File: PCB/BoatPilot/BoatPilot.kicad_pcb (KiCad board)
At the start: 2 copper layers, 40 x 40 mm, 83 parts, among them J101 battery, J102 switch, J103 SWD, J104 wind, J105 RC, J106 GPS, J108 failsafe, J109 SERVO1, J110 SERVO2, J111 SERVO3, J201 GPIO, J202 USB-Audio-IR, J203 Audio-UART, P101 ICT-Point, P102 ICT-Point, P103 ICT-Point, P104 ICT-Point, P105 ICT-Point, P113 ICT-Point, P119 ICT-Point, P129 ICT-Point, P130 ICT-Point, P132 ICT-Point, P133 ICT-Point, P134 ICT-Point, P135 ICT-Point, Q101 TSM3457, U101 GY-91, U102 74LVC1G97, U103 LM1117-3.3, U104 TPS565208, U105 24LC512, U106 74LVC1G97, U108 74LVC1G97, U109 STM32F103C8Tx, Y101 8MHz

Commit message: Finish documentation
Documentation layer finished
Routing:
- net GND: vias 79 -> 75

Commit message: Move Servo outputs
Move servo outputs so that only a single Timer (TIM2) is needed to
gerenarte the PWM with the Capture Compare units.
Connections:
- J201 pad 10: (no net) -> /FriednlyARM NanoPi Air/RX1
- J201 pad 13: (no net) -> /FriednlyARM NanoPi Air/RTS2_PA2
- J201 pad 15: (no net) -> /FriednlyARM NanoPi Air/CTS2_PA3
- J201 pad 16: (no net) -> /FriednlyARM NanoPi Air/RTS1
- J201 pad 18: (no net) -> /FriednlyARM NanoPi Air/CTS1
- J201 pad 7: (no net) -> /FriednlyARM NanoPi Air/PG11
- J201 pad 8: (no net) -> /FriednlyARM NanoPi Air/TX1
- J202 pad 10: (no net) -> /FriednlyARM NanoPi Air/I2S_DOUT
- J202 pad 11: (no net) -> /FriednlyARM NanoPi Air/I2S_DIN
- J202 pad 2: (no net) -> /FriednlyARM NanoPi Air/D1P
- J202 pad 3: (no net) -> /FriednlyARM NanoPi Air/D1N
- J202 pad 6: (no net) -> /FriednlyARM NanoPi Air/PL11_IR
- J202 pad 7: (no net) -> /FriednlyARM NanoPi Air/PA17_SPDIF
- J202 pad 8: (no net) -> /FriednlyARM NanoPi Air/I2S_LRCK
- J202 pad 9: (no net) -> /FriednlyARM NanoPi Air/I2S_BCK
- J203 pad 3: (no net) -> /FriednlyARM NanoPi Air/TX0
- J203 pad 4: (no net) -> /FriednlyARM NanoPi Air/RX0
- J203 pad 5: (no net) -> /FriednlyARM NanoPi Air/LL
- J203 pad 6: (no net) -> /FriednlyARM NanoPi Air/LR
- J203 pad 7: (no net) -> /FriednlyARM NanoPi Air/MN
- J203 pad 8: (no net) -> /FriednlyARM NanoPi Air/MP
- U101 pad 1: (no net) -> Net-(U101-Pad1)
- U109 pad 11: (no net) -> Net-(U109-Pad11)
- U109 pad 18: (no net) -> Net-(U109-Pad18)
- U109 pad 19: (no net) -> Net-(U109-Pad19)
- U109 pad 2: (no net) -> Net-(U109-Pad2)
- U109 pad 20: (no net) -> Net-(U109-Pad20)
- U109 pad 21: (no net) -> Net-(U109-Pad21)
- U109 pad 22: (no net) -> Net-(U109-Pad22)
- U109 pad 25: (no net) -> Net-(U109-Pad25)
- U109 pad 3: (no net) -> Net-(U109-Pad3)
- U109 pad 38: (no net) -> Net-(U109-Pad38)
- U109 pad 4: (no net) -> Net-(U109-Pad4)
- U109 pad 46: (no net) -> Net-(U109-Pad46)
- Y101 pad 2: (no net) -> Net-(Y101-Pad2)
- Y101 pad 4: (no net) -> Net-(Y101-Pad4)
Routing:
- net GND: track 70.7 -> 72.0 mm

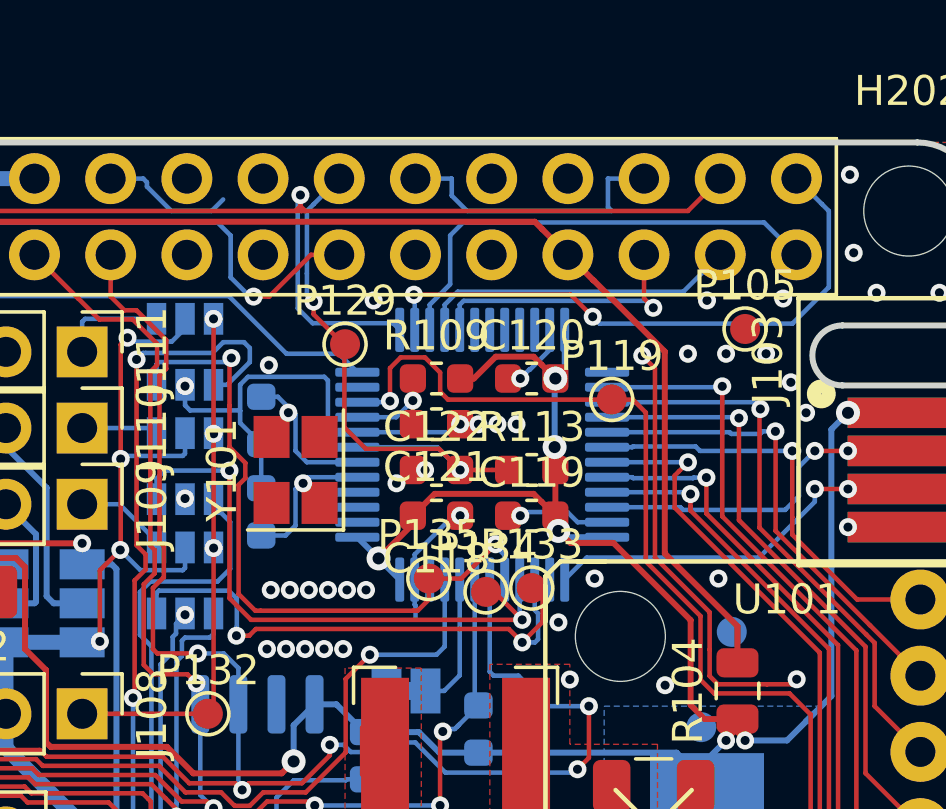
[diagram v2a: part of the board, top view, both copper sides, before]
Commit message: Route new servo connections
Reroute parts of the PCB to fit the new servo connections
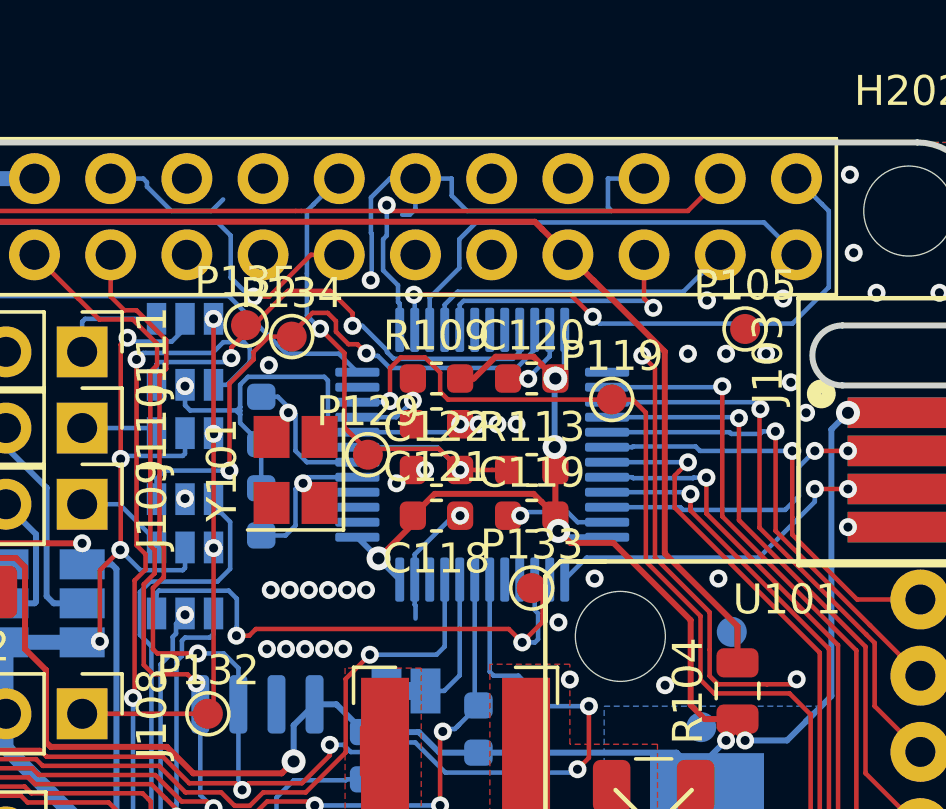
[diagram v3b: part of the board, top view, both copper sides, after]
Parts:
- moved P134 10.7 mm to (141.1, 85.5)
- moved P135 10.4 mm to (139.6, 85.1)
- moved P129 3.76 mm to (143.7, 89.4)
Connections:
- J201 pad 10: /FriednlyARM NanoPi Air/RX1 -> (no net)
- J201 pad 13: /FriednlyARM NanoPi Air/RTS2_PA2 -> (no net)
- J201 pad 15: /FriednlyARM NanoPi Air/CTS2_PA3 -> (no net)
- J201 pad 16: /FriednlyARM NanoPi Air/RTS1 -> (no net)
- J201 pad 18: /FriednlyARM NanoPi Air/CTS1 -> (no net)
- J201 pad 7: /FriednlyARM NanoPi Air/PG11 -> (no net)
- J201 pad 8: /FriednlyARM NanoPi Air/TX1 -> (no net)
- J202 pad 10: /FriednlyARM NanoPi Air/I2S_DOUT -> (no net)
- J202 pad 11: /FriednlyARM NanoPi Air/I2S_DIN -> (no net)
- J202 pad 2: /FriednlyARM NanoPi Air/D1P -> (no net)
- J202 pad 3: /FriednlyARM NanoPi Air/D1N -> (no net)
- J202 pad 6: /FriednlyARM NanoPi Air/PL11_IR -> (no net)
- J202 pad 7: /FriednlyARM NanoPi Air/PA17_SPDIF -> (no net)
- J202 pad 8: /FriednlyARM NanoPi Air/I2S_LRCK -> (no net)
- J202 pad 9: /FriednlyARM NanoPi Air/I2S_BCK -> (no net)
- J203 pad 3: /FriednlyARM NanoPi Air/TX0 -> (no net)
- J203 pad 4: /FriednlyARM NanoPi Air/RX0 -> (no net)
- J203 pad 5: /FriednlyARM NanoPi Air/LL -> (no net)
- J203 pad 6: /FriednlyARM NanoPi Air/LR -> (no net)
- J203 pad 7: /FriednlyARM NanoPi Air/MN -> (no net)
- J203 pad 8: /FriednlyARM NanoPi Air/MP -> (no net)
- U101 pad 1: Net-(U101-Pad1) -> (no net)
- U109 pad 11: Net-(U109-Pad11) -> (no net)
- U109 pad 18: Net-(U109-Pad18) -> (no net)
- U109 pad 19: Net-(U109-Pad19) -> (no net)
- U109 pad 2: Net-(U109-Pad2) -> (no net)
- U109 pad 20: Net-(U109-Pad20) -> (no net)
- U109 pad 21: Net-(U109-Pad21) -> /SERVO3
- U109 pad 22: Net-(U109-Pad22) -> /SERVO1
- U109 pad 25: Net-(U109-Pad25) -> (no net)
- U109 pad 3: Net-(U109-Pad3) -> (no net)
- U109 pad 38: Net-(U109-Pad38) -> (no net)
- U109 pad 4: Net-(U109-Pad4) -> (no net)
- U109 pad 40: /SERVO1 -> (no net)
- U109 pad 41: /SERVO3 -> (no net)
- U109 pad 46: Net-(U109-Pad46) -> (no net)
- Y101 pad 2: Net-(Y101-Pad2) -> (no net)
- Y101 pad 4: Net-(Y101-Pad4) -> (no net)
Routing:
- net GND: track 72.0 -> 79.6 mm
- net /SERVO3: track 22.9 -> 16.5 mm
- net /UART2_RX: track 49.4 -> 45.5 mm
- net /SERVO1: track 20.5 -> 19.4 mm

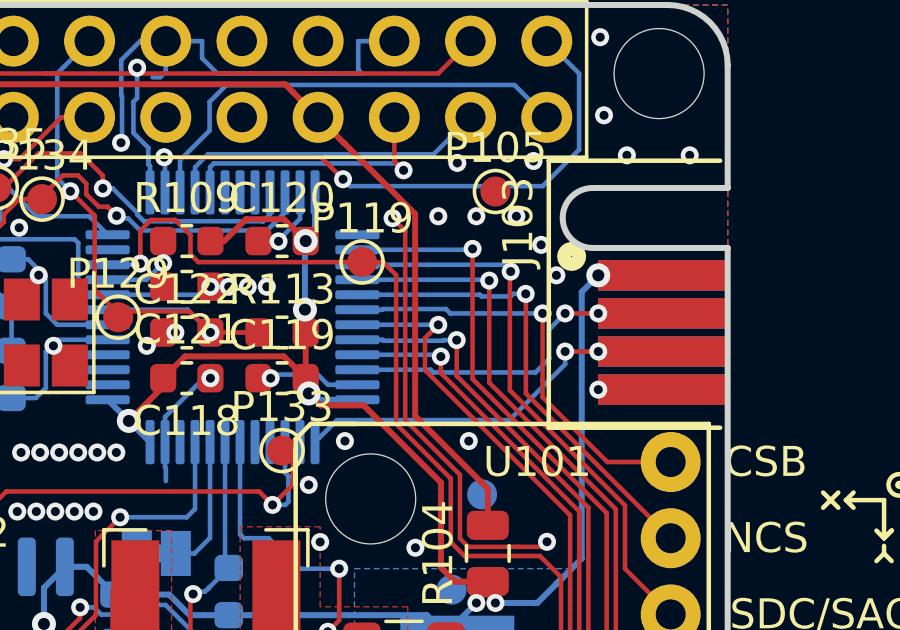
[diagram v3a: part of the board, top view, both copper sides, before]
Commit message: Swap UART1 RX and TX to enable half duplex mode
In half duplex mode, UART RX can be used as a GPIO pin. So the pinning
on the uC has to be swapped.
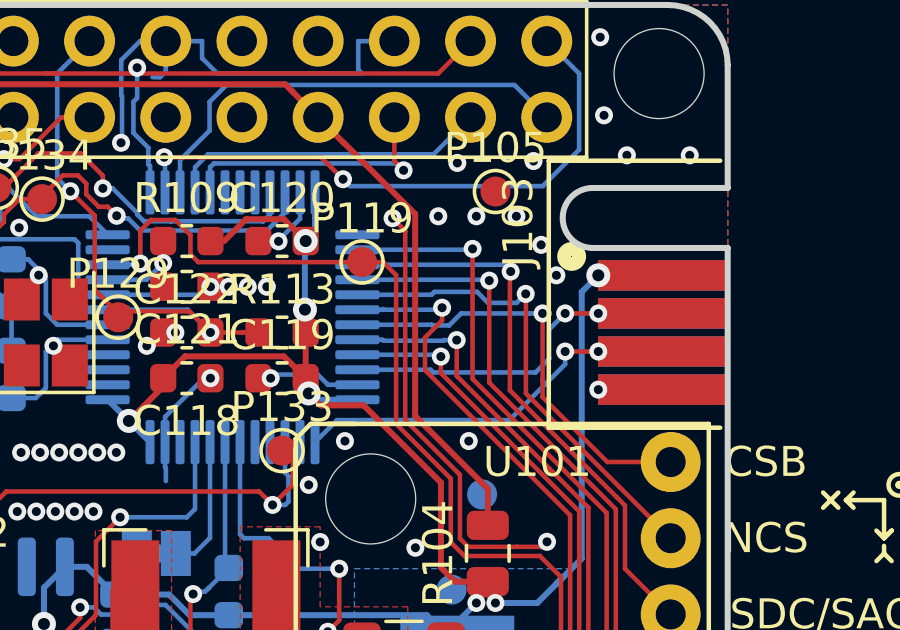
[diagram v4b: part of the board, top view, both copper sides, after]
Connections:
- J201 pad 10: (no net) -> /FriednlyARM NanoPi Air/RX1
- J201 pad 13: (no net) -> /FriednlyARM NanoPi Air/RTS2_PA2
- J201 pad 15: (no net) -> /FriednlyARM NanoPi Air/CTS2_PA3
- J201 pad 16: (no net) -> /FriednlyARM NanoPi Air/RTS1
- J201 pad 18: (no net) -> /FriednlyARM NanoPi Air/CTS1
- J201 pad 7: (no net) -> /FriednlyARM NanoPi Air/PG11
- J201 pad 8: (no net) -> /FriednlyARM NanoPi Air/TX1
- J202 pad 10: (no net) -> /FriednlyARM NanoPi Air/I2S_DOUT
- J202 pad 11: (no net) -> /FriednlyARM NanoPi Air/I2S_DIN
- J202 pad 2: (no net) -> /FriednlyARM NanoPi Air/D1P
- J202 pad 3: (no net) -> /FriednlyARM NanoPi Air/D1N
- J202 pad 6: (no net) -> /FriednlyARM NanoPi Air/PL11_IR
- J202 pad 7: (no net) -> /FriednlyARM NanoPi Air/PA17_SPDIF
- J202 pad 8: (no net) -> /FriednlyARM NanoPi Air/I2S_LRCK
- J202 pad 9: (no net) -> /FriednlyARM NanoPi Air/I2S_BCK
- J203 pad 3: (no net) -> /FriednlyARM NanoPi Air/TX0
- J203 pad 4: (no net) -> /FriednlyARM NanoPi Air/RX0
- J203 pad 5: (no net) -> /FriednlyARM NanoPi Air/LL
- J203 pad 6: (no net) -> /FriednlyARM NanoPi Air/LR
- J203 pad 7: (no net) -> /FriednlyARM NanoPi Air/MN
- J203 pad 8: (no net) -> /FriednlyARM NanoPi Air/MP
- U101 pad 1: (no net) -> Net-(U101-Pad1)
- U109 pad 11: (no net) -> Net-(U109-Pad11)
- U109 pad 18: (no net) -> Net-(U109-Pad18)
- U109 pad 19: (no net) -> Net-(U109-Pad19)
- U109 pad 2: (no net) -> Net-(U109-Pad2)
- U109 pad 20: (no net) -> Net-(U109-Pad20)
- U109 pad 25: (no net) -> Net-(U109-Pad25)
- U109 pad 3: (no net) -> Net-(U109-Pad3)
- U109 pad 30: /~CS_MPU9250 -> /RC_IBUS
- U109 pad 31: /RC_IBUS -> /~CS_MPU9250
- U109 pad 38: (no net) -> Net-(U109-Pad38)
- U109 pad 4: (no net) -> Net-(U109-Pad4)
- U109 pad 40: (no net) -> Net-(U109-Pad40)
- U109 pad 41: (no net) -> Net-(U109-Pad41)
- U109 pad 46: (no net) -> Net-(U109-Pad46)
- Y101 pad 2: (no net) -> Net-(Y101-Pad2)
- Y101 pad 4: (no net) -> Net-(Y101-Pad4)
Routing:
- net /RC_IBUS: track 54.1 -> 54.9 mm

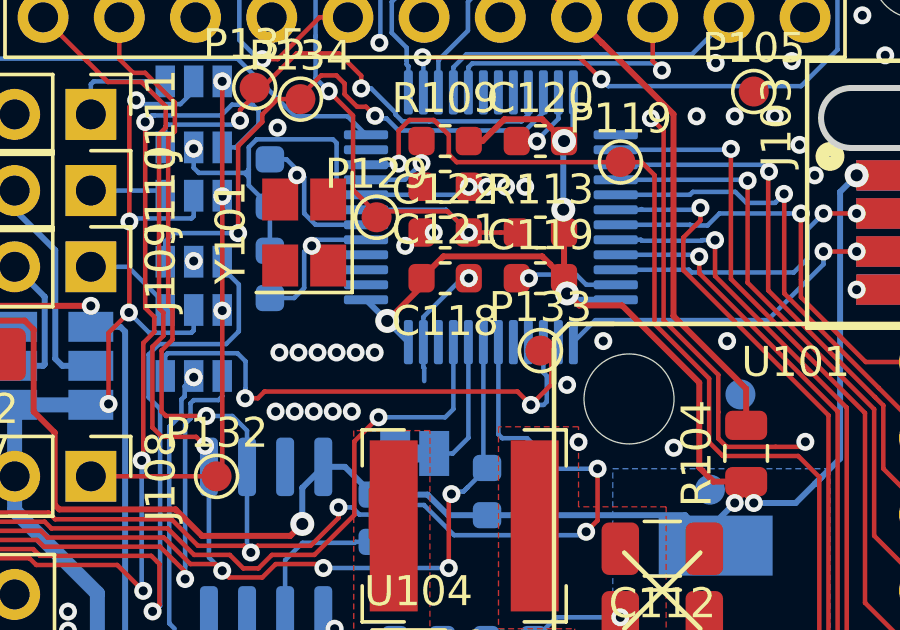
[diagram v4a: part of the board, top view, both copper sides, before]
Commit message: Add test points for a software serial port
Update the layout to have a SW UART (3,3V, TX, RX, GND)
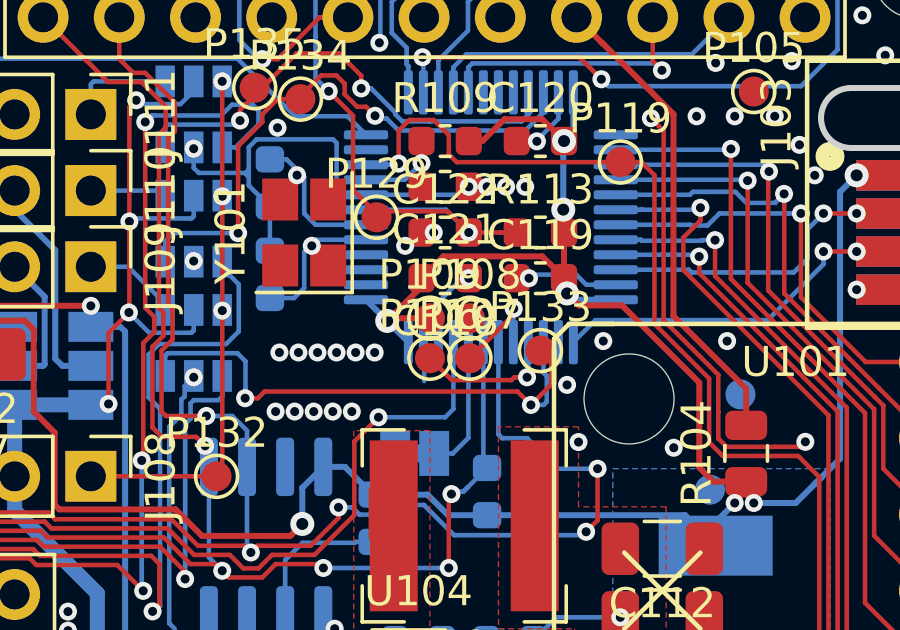
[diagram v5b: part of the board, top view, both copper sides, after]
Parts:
- added P106: ICT-Point, TestPoint:TestPoint_Pad_D1.0mm, F.Cu at (145.5, 94.1)
- added P107: ICT-Point, TestPoint:TestPoint_Pad_D1.0mm, F.Cu at (146.8, 94.1)
- added P108: ICT-Point, TestPoint:TestPoint_Pad_D1.0mm, F.Cu at (146.8, 92.8)
- added P109: ICT-Point, TestPoint:TestPoint_Pad_D1.0mm, F.Cu at (145.5, 92.8)
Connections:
- U109 pad 40: Net-(U109-Pad40) -> /DEBUG_TX
- U109 pad 41: Net-(U109-Pad41) -> /DEBUG_RX
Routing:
- net /DEBUG_TX: track 0.00 -> 4.77 mm, vias 0 -> 1
- net /DEBUG_RX: track 0.00 -> 3.38 mm, vias 0 -> 1
- net +3V3: track 119.5 -> 121.4 mm
